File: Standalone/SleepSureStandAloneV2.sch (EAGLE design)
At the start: 60 parts, among them IC1 CP2104, Q1 mmbt2222, Q2 mmbt2222, Q3 DMG3415U, SW2 KMR2, U1 ADS1299-4PAG, U2 AP2112-3.3, U3 MCP73831T-2ACI/OT, X1 JSTPH, X2 ESP32_WROOM32_SKINNY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

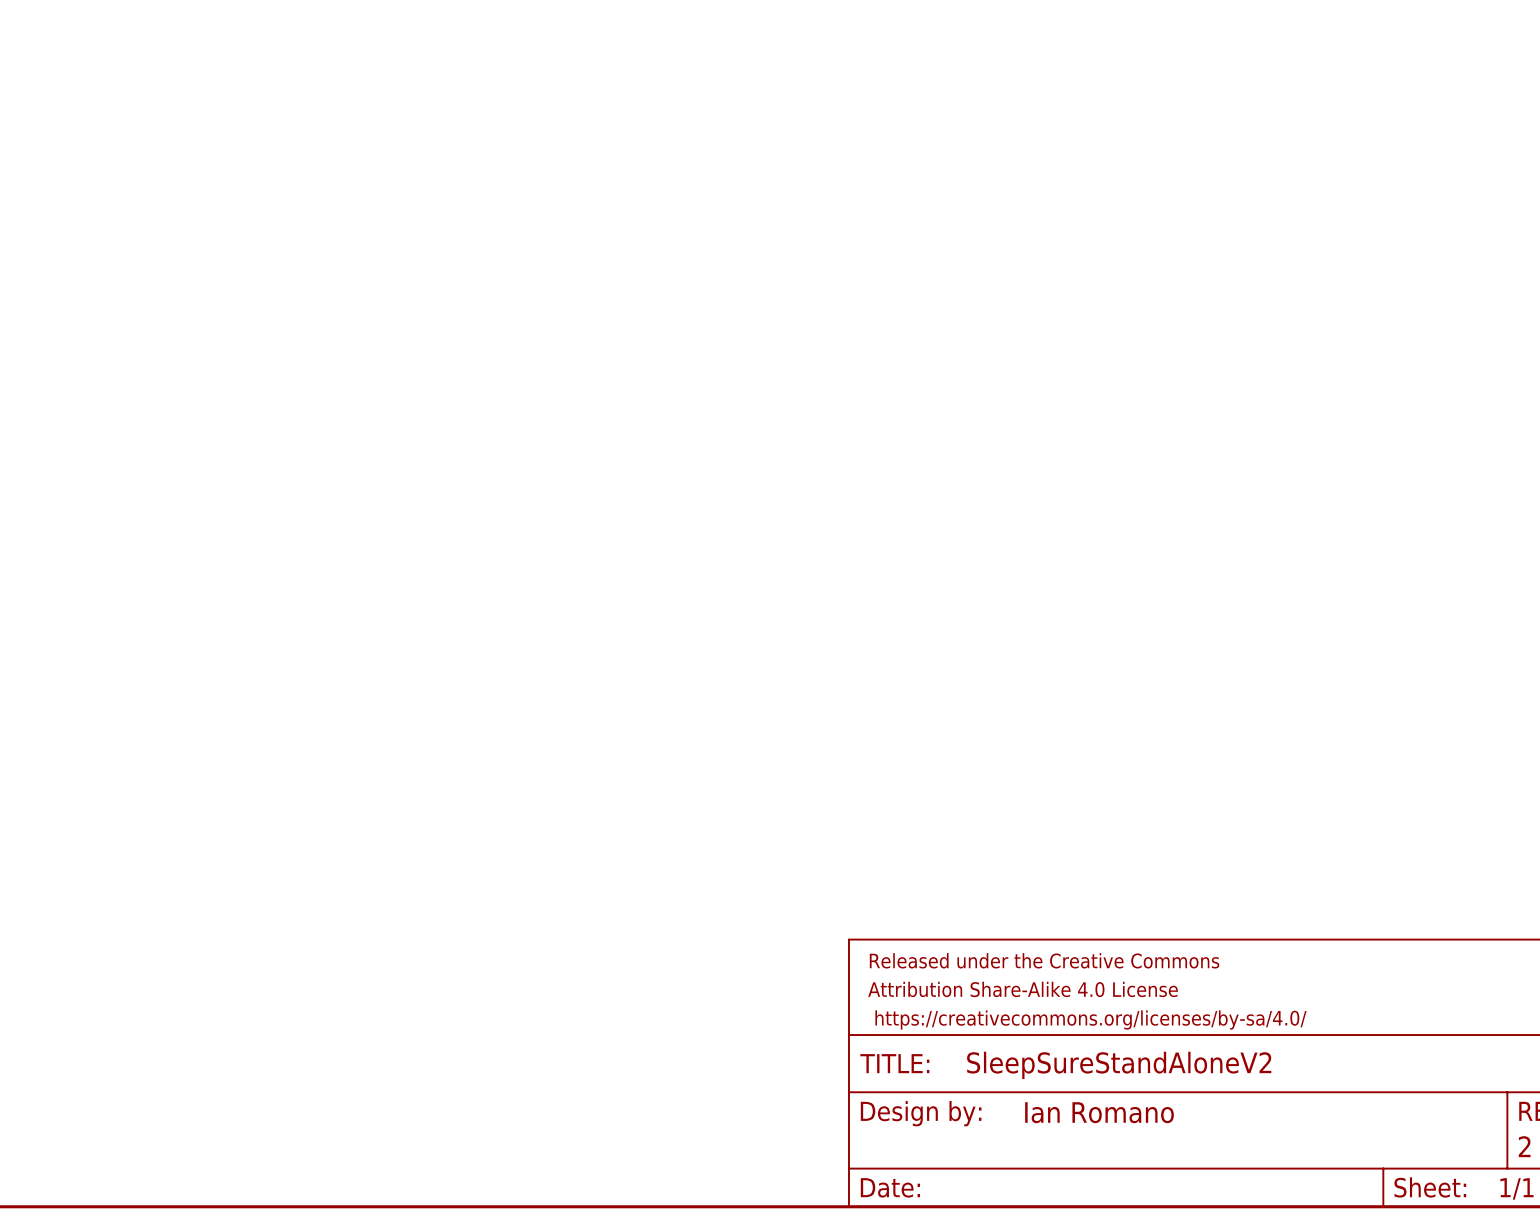
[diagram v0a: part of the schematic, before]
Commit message: Added power booster to standalone board
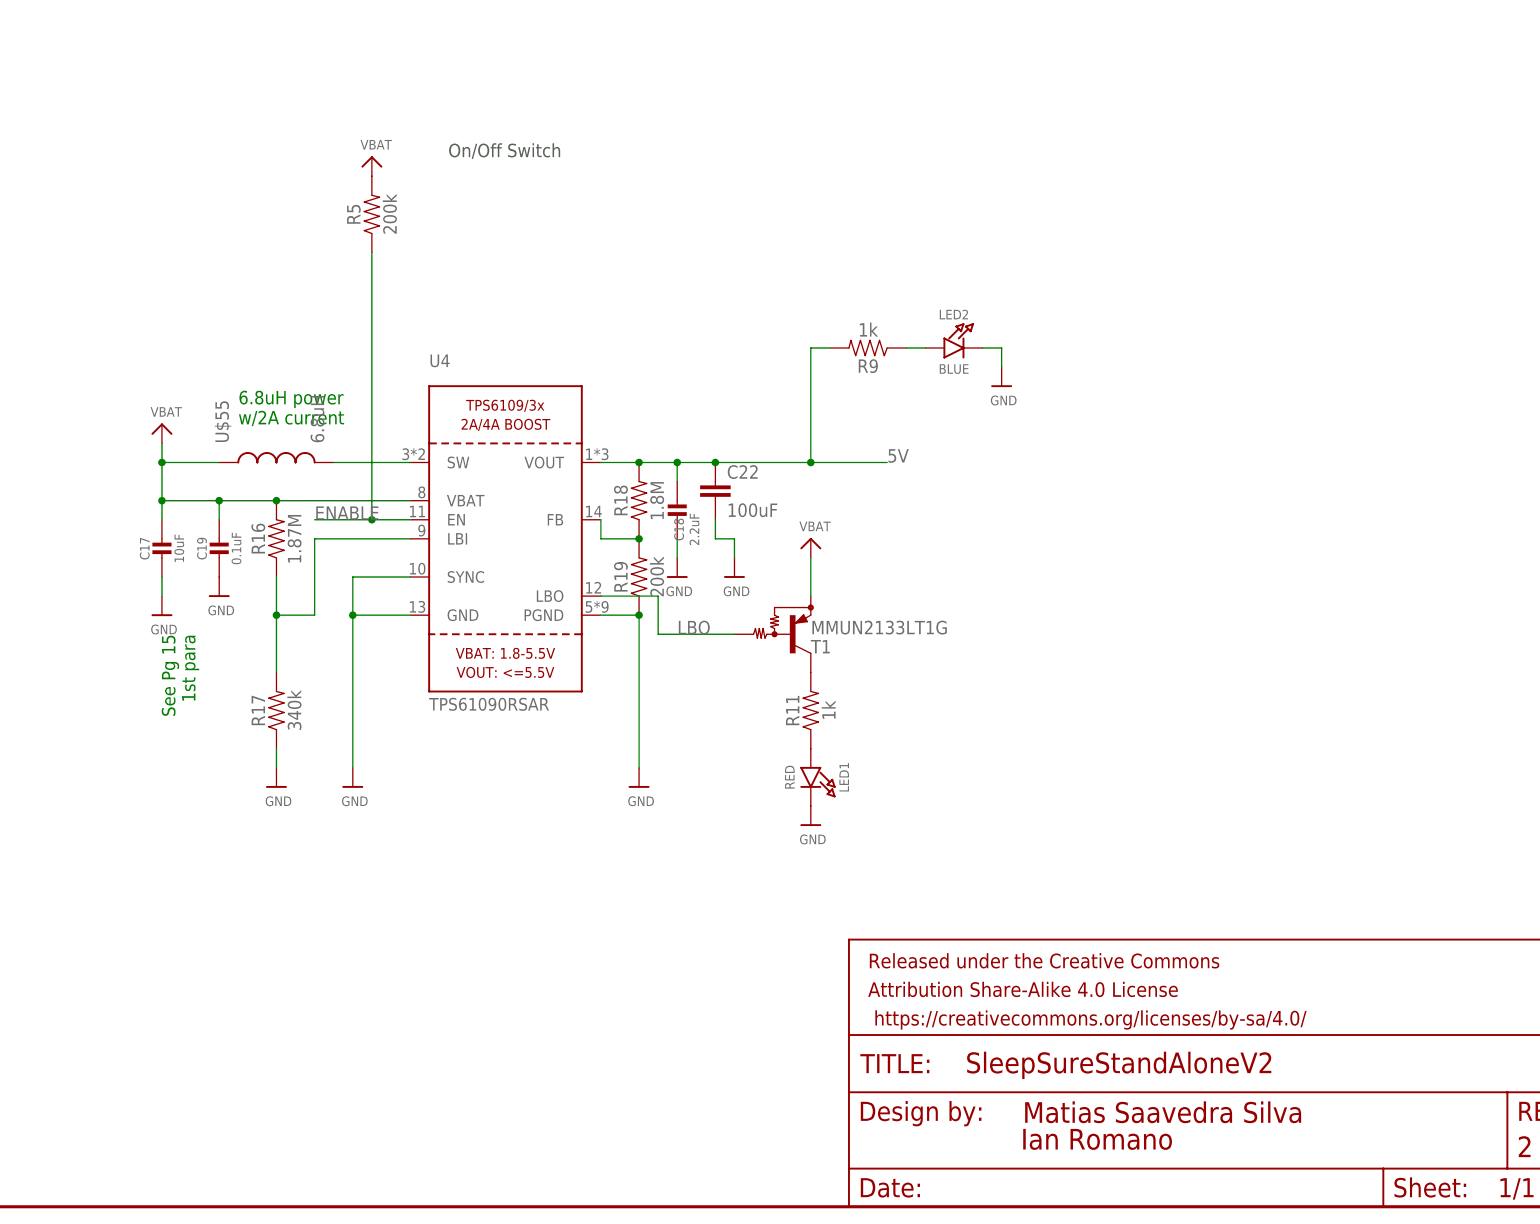
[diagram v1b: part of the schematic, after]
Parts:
- added C17: 10uF, microbuilder:CAP_CERAMIC0805-NOOUTLINE
- added C18: 2.2uF, microbuilder:CAP_CERAMIC0805-NOOUTLINE
- added C19: 0.1uF, microbuilder:CAP_CERAMIC0805_10MGAP
- added C22: 100uF, SparkFun-Capacitors:10UF-0805-10V-10%
- added LED1: RED, microbuilder:LED0805_NOOUTLINE
- added LED2: BLUE, microbuilder:LED0805_NOOUTLINE
- added R11, R9: 1k, SparkFun-Resistors:RESISTOR0805
- added R16: 1.87M, SparkFun-Resistors:RESISTOR0805
- added R17: 340k, SparkFun-Resistors:RESISTOR0805
- added R18: 1.8M, SparkFun-Resistors:RESISTOR0805
- added R19, R5: 200k, SparkFun-Resistors:RESISTOR0805
- added T1: MMUN2133LT1G, transistor:MUN2114T1-PNP_DRIVER-SC59-BEC
- added U$55: 6.8uH, ADS_Feather:ASPI-0628-6R8M-T1
- added U4: TPS61090RSAR, microbuilder:VREG_TPS6103X
- FRAME2: DESIGNER Ian Romano -> Matias Saavedra Silva; DESIGNER2 (none) -> Ian Romano
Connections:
- new net ENABLE: R5.1, U4.EN
- new net LBO: T1.B, U4.LBO
- new net N$16: U$55.2, U4.SW
- new net N$17: R16.1, R17.2, U4.LBI
- new net N$18: R18.1, R19.2, U4.FB
- new net N$19: LED2.A, R9.1
- new net N$20: LED1.A, R11.1
- new net N$21: R11.2, T1.C
- net 5V: now also C18.1, C22.1, R18.2, R9.2, U4.VOUT
- net GND: now also C17.2, C18.2, C19.2, C22.2, LED1.C, LED2.C, R17.1, R19.1, U4.GND, U4.PGND, U4.SYNC
- net VBAT: now also C17.1, C19.1, R16.2, R5.2, T1.E, U$55.1, U4.VBAT
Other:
- note added: "6.8uH power w/2A current"
- note added: "On/Off Switch"
- note added: "See Pg 15 1st para"

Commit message: changed usb header'
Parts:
- removed X4: 20329, microbuilder:USB_MICRO_20329_V2
- added J1: 10118192-0002LF, ADS_Feather:10118192-0002LF
- added U$62, U$66: (no value), ADS_Feather:MBR160HW
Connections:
- removed net N$2: IC1G$1.D+, X4.D+
- removed net N$6: IC1G$1.D-, X4.D-
- new net 5VBAT: C18.1, C22.1, R18.2, R9.2, U$66.A, U4.VOUT
- new net D+: IC1G$1.D+, J1.D+
- new net D-: IC1G$1.D-, J1.D-
- net 5V: now also U$62.C, U$66.C; no longer C18.1, C22.1, R18.2, R9.2, U4.VOUT
- net GND: now also J1.GND; no longer X4.GND
- net VBUS: now also J1.VCC, U$62.A; no longer X4.VBUS

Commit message: modified design file and removed errors
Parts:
- U$23, U$46, U$48, U$50, U$52: value W2A45C103MAT2A -> 1nF
- U$44, U$45, U$47, U$49, U$51: value (none) -> 2.2k
- U$62, U$66: value (none) -> MRB120
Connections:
- removed net IO14_A6: X2.IO14/A2_6
- removed net IO15_A8: X2.IO15/A2_3
- removed net IO32_A7: X2.IO32/A1_4/X32P
- removed net SCLK: U1.SCLK
- new net GPIO0: Q2.C, X2.IO0/A2_1
- new net IO16: X2.IO16
- net ADS_CS: now also X2.IO14/A2_6; no longer Q2.C, X2.IO0/A2_1
- net ADS_RESET: now also X2.IO32/A1_4/X32P
- net DRDY: now also X2.IO15/A2_3; no longer X2.IO16
- net SCK: now also U1.SCLK
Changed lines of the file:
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@@
 <setting verticaltext="up"/>
 </settings>
-<grid distance="0.1" unitdist="inch" unit="inch" style="lines" multiple="1" display="yes" altdistance="0.01" altunitdist="inch" altunit="inch"/>
+<grid distance="0.1" unitdist="inch" unit="inch" style="lines" multiple="1" display="no" altdistance="0.01" altunitdist="inch" altunit="inch"/>
 <layers>
 <layer number="1" name="Top" color="4" fill="1" visible="no" active="no"/>
@@
 <part name="R20" library="SparkFun-Resistors" deviceset="RESISTOR" device="0805" value="1M"/>
 <part name="JP2" library="SleepSureLib" deviceset="PINHD-2X10" device="-BIG" package3d_urn="urn:adsk.eagle:package:6240766/1"/>
-<part name="U$44" library="SleepSureLib" deviceset="EXB-28V222JX" device=""/>
-<part name="U$23" library="SleepSureLib" deviceset="W2A45C103MAT2A" device=""/>
-<part name="U$45" library="SleepSureLib" deviceset="EXB-28V222JX" device=""/>
-<part name="U$46" library="SleepSureLib" deviceset="W2A45C103MAT2A" device=""/>
-<part name="U$47" library="SleepSureLib" deviceset="EXB-28V222JX" device=""/>
-<part name="U$48" library="SleepSureLib" deviceset="W2A45C103MAT2A" device=""/>
-<part name="U$49" library="SleepSureLib" deviceset="EXB-28V222JX" device=""/>
-<part name="U$50" library="SleepSureLib" deviceset="W2A45C103MAT2A" device=""/>
-<part name="U$51" library="SleepSureLib" deviceset="EXB-28V222JX" device=""/>
-<part name="U$52" library="SleepSureLib" deviceset="W2A45C103MAT2A" device=""/>
+<part name="U$44" library="SleepSureLib" deviceset="EXB-28V222JX" device="" value="2.2k"/>
+<part name="U$23" library="SleepSureLib" deviceset="W2A45C103MAT2A" device="" value="1nF"/>
+<part name="U$45" library="SleepSureLib" deviceset="EXB-28V222JX" device="" value="2.2k"/>
+<part name="U$46" library="SleepSureLib" deviceset="W2A45C103MAT2A" device="" value="1nF"/>
+<part name="U$47" library="SleepSureLib" deviceset="EXB-28V222JX" device="" value="2.2k"/>
+<part name="U$48" library="SleepSureLib" deviceset="W2A45C103MAT2A" device="" value="1nF"/>
+<part name="U$49" library="SleepSureLib" deviceset="EXB-28V222JX" device="" value="2.2k"/>
+<part name="U$50" library="SleepSureLib" deviceset="W2A45C103MAT2A" device="" value="1nF"/>
+<part name="U$51" library="SleepSureLib" deviceset="EXB-28V222JX" device="" value="2.2k"/>
+<part name="U$52" library="SleepSureLib" deviceset="W2A45C103MAT2A" device="" value="1nF"/>
 <part name="U$6" library="microbuilder" deviceset="MOUNTINGHOLE" device="2.5"/>
 <part name="U$19" library="microbuilder" deviceset="MOUNTINGHOLE" device="2.5"/>
@@
 <part name="U$55" library="ADS_Feather" deviceset="ASPI-0628-6R8M-T1" device="" value="6.8uH"/>
 <part name="R5" library="SparkFun-Resistors" deviceset="RESISTOR" device="0805" value="200k"/>
-<part name="U$62" library="ADS_Feather" deviceset="MBR160HW" device=""/>
-<part name="U$66" library="ADS_Feather" deviceset="MBR160HW" device=""/>
+<part name="U$62" library="ADS_Feather" deviceset="MBR160HW" device="" value="MRB120"/>
+<part name="U$66" library="ADS_Feather" deviceset="MBR160HW" device="" value="MRB120"/>
 <part name="J1" library="ADS_Feather" deviceset="10118192-0002LF" device=""/>
 </parts>
@@
 </instance>
 <instance part="U$12" gate="G$1" x="185.42" y="134.62" smashed="yes">
-<attribute name="VALUE" x="183.896" y="132.08" size="1.27" layer="96"/>
+<attribute name="VALUE" x="183.896" y="134.62" size="1.27" layer="96"/>
 </instance>
 <instance part="C2" gate="G$1" x="180.34" y="142.24" smashed="yes">
@@
 </instance>
 <instance part="U$17" gate="G$1" x="180.34" y="134.62" smashed="yes">
-<attribute name="VALUE" x="178.816" y="132.08" size="1.27" layer="96"/>
+<attribute name="VALUE" x="178.816" y="134.62" size="1.27" layer="96"/>
 </instance>
 <instance part="U$18" gate="G$1" x="172.72" y="134.62" smashed="yes">
@@
 </segment>
 </net>
-<net name="IO32_A7" class="0">
-<segment>
-<wire x1="78.74" y1="71.12" x2="91.44" y2="71.12" width="0.1524" layer="91"/>
-<label x="81.28" y="71.12" size="1.778" layer="95"/>
-<pinref part="X2" gate="G$1" pin="IO32/A1_4/X32P"/>
-</segment>
-</net>
 <net name="IO27_A10" class="0">
 <segment>
@@
 <label x="81.28" y="109.22" size="1.778" layer="95"/>
 <pinref part="X2" gate="G$1" pin="IO5"/>
+</segment>
+<segment>
+<pinref part="U1" gate="G$1" pin="SCLK"/>
+<wire x1="-340.36" y1="53.34" x2="-365.76" y2="53.34" width="0.1524" layer="91"/>
+<label x="-365.76" y="53.34" size="1.778" layer="95"/>
 </segment>
 </net>
@@
 </segment>
 </net>
-<net name="IO15_A8" class="0">
-<segment>
-<wire x1="78.74" y1="99.06" x2="91.44" y2="99.06" width="0.1524" layer="91"/>
-<label x="81.28" y="99.06" size="1.778" layer="95"/>
-<pinref part="X2" gate="G$1" pin="IO15/A2_3"/>
-</segment>
-</net>
 <net name="IO21" class="0">
 <segment>
@@
 </segment>
 </net>
-<net name="IO14_A6" class="0">
-<segment>
-<wire x1="78.74" y1="101.6" x2="91.44" y2="101.6" width="0.1524" layer="91"/>
-<label x="81.28" y="101.6" size="1.778" layer="95"/>
-<pinref part="X2" gate="G$1" pin="IO14/A2_6"/>
-</segment>
-</net>
-<net name="SCLK" class="0">
-<segment>
-<pinref part="U1" gate="G$1" pin="SCLK"/>
-<wire x1="-340.36" y1="53.34" x2="-365.76" y2="53.34" width="0.1524" layer="91"/>
-<label x="-365.76" y="53.34" size="1.778" layer="95"/>
-</segment>
-</net>
 <net name="CLK0" class="0">
 <segment>
@@
 <wire x1="-340.36" y1="116.84" x2="-365.76" y2="116.84" width="0.1524" layer="91"/>
 <label x="-365.76" y="116.84" size="1.778" layer="95"/>
+</segment>
+<segment>
+<wire x1="78.74" y1="71.12" x2="91.44" y2="71.12" width="0.1524" layer="91"/>
+<label x="81.28" y="71.12" size="1.778" layer="95"/>
+<pinref part="X2" gate="G$1" pin="IO32/A1_4/X32P"/>
 </segment>
 </net>
@@
 </segment>
 <segment>
-<wire x1="78.74" y1="96.52" x2="91.44" y2="96.52" width="0.1524" layer="91"/>
-<label x="81.28" y="96.52" size="1.778" layer="95"/>
-<pinref part="X2" gate="G$1" pin="IO16"/>
+<wire x1="78.74" y1="99.06" x2="91.44" y2="99.06" width="0.1524" layer="91"/>
+<label x="81.28" y="99.06" size="1.778" layer="95"/>
+<pinref part="X2" gate="G$1" pin="IO15/A2_3"/>
 </segment>
 </net>
 <net name="ADS_CS" class="0">
-<segment>
-<wire x1="78.74" y1="116.84" x2="91.44" y2="116.84" width="0.1524" layer="91"/>
-<label x="81.28" y="116.84" size="1.778" layer="95"/>
-<pinref part="X2" gate="G$1" pin="IO0/A2_1"/>
-</segment>
 <segment>
 <pinref part="U1" gate="G$1" pin="!CS"/>
@@
 </segment>
 <segment>
-<wire x1="124.46" y1="86.36" x2="137.16" y2="86.36" width="0.1524" layer="91"/>
-<label x="127" y="86.36" size="1.778" layer="95"/>
-<pinref part="Q2" gate="G$1" pin="C"/>
+<wire x1="78.74" y1="101.6" x2="91.44" y2="101.6" width="0.1524" layer="91"/>
+<label x="81.28" y="101.6" size="1.778" layer="95"/>
+<pinref part="X2" gate="G$1" pin="IO14/A2_6"/>
 </segment>
 </net>
@@
 </segment>
 </net>
+<net name="GPIO0" class="0">
+<segment>
+<pinref part="X2" gate="G$1" pin="IO0/A2_1"/>
+<wire x1="78.74" y1="116.84" x2="91.44" y2="116.84" width="0.1524" layer="91"/>
+<label x="81.28" y="116.84" size="1.778" layer="95"/>
+</segment>
+<segment>
+<pinref part="Q2" gate="G$1" pin="C"/>
+<wire x1="124.46" y1="86.36" x2="137.16" y2="86.36" width="0.1524" layer="91"/>
+<label x="127" y="86.36" size="1.778" layer="95"/>
+</segment>
+</net>
+<net name="IO16" class="0">
+<segment>
+<pinref part="X2" gate="G$1" pin="IO16"/>
+<wire x1="78.74" y1="96.52" x2="91.44" y2="96.52" width="0.1524" layer="91"/>
+<label x="81.28" y="96.52" size="1.778" layer="95"/>
+</segment>
+</net>
